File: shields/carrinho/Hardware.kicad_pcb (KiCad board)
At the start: 2 copper layers, 133.4 x 56.1 mm, 78 parts, among them J1 Conn_02x02_Odd_Even, J10 Conn_01x04, J11 Conn_01x04, J12 Conn_02x13_Odd_Even, J2 Conn_01x04, J3 Conn_02x02_Odd_Even, J4 Conn_01x02_Male, J5 Conn_01x02_Male, J6 Conn_01x02_Male, J7 Conn_01x02_Male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

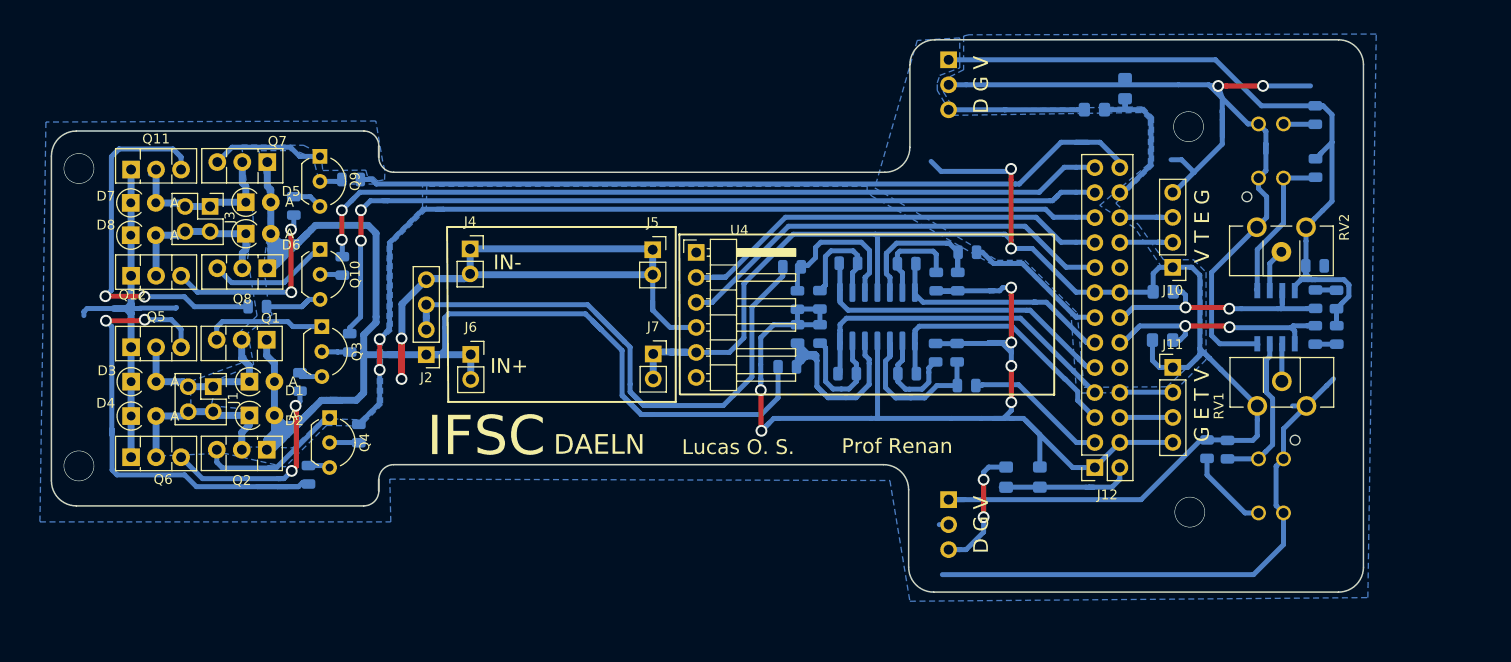
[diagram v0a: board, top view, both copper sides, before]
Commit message: Changed motors conector, added capacitor near ampop
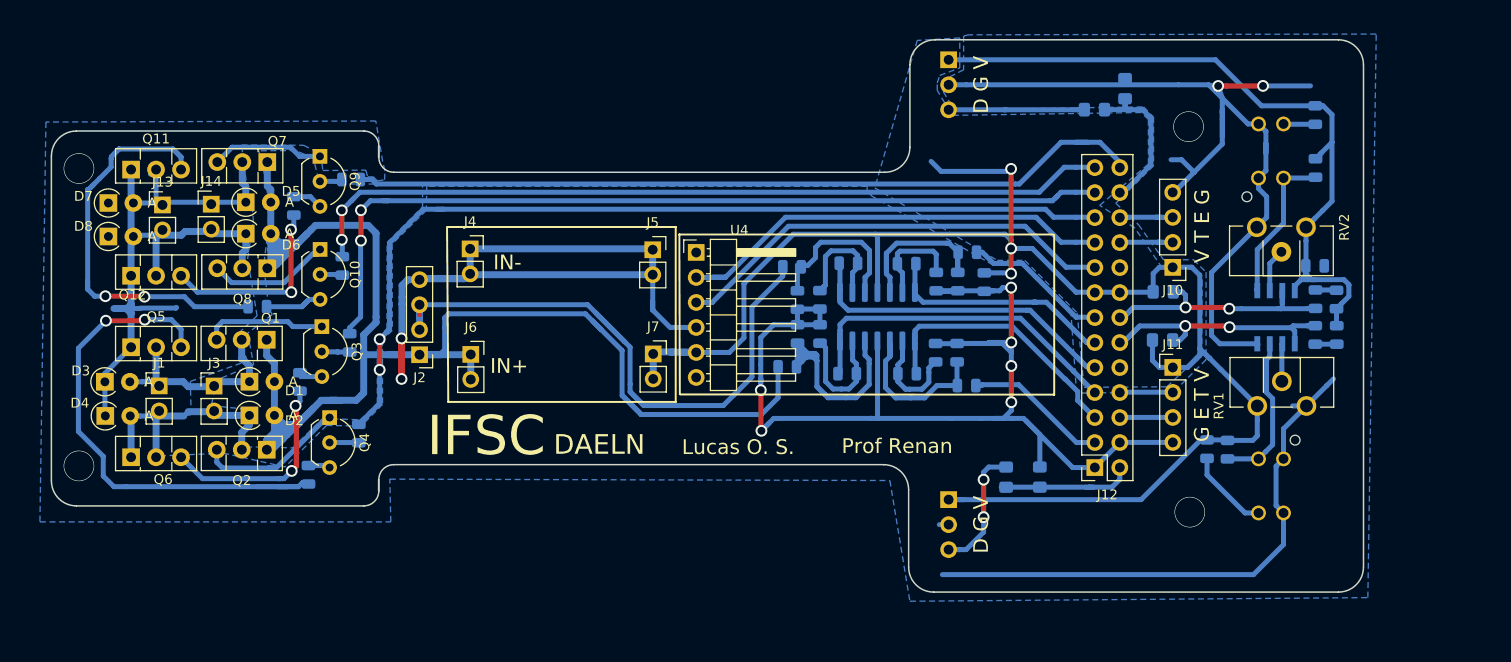
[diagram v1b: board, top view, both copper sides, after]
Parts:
- added C4: 100n, Capacitor_SMD:C_0805_2012Metric, B.Cu at (225.0, 56.4)
- added J13: Conn_01x02, Connector_PinHeader_2.54mm:PinHeader_1x02_P2.54mm_Vertical, F.Cu at (141.5, 48.5)
- added J14: Conn_01x02, Connector_PinHeader_2.54mm:PinHeader_1x02_P2.54mm_Vertical, F.Cu at (146.5, 48.5)
- C1, C2: value C -> 1n
- C3: value C -> 100n
- J1, J3: value Conn_02x02_Odd_Even -> Conn_01x02; footprint Connector_PinHeader_2.54mm:PinHeader_2x02_P2.54mm_Vertical -> Connector_PinHeader_2.54mm:PinHeader_1x02_P2.54mm_Vertical
- R31, R32: value R -> 10k
- moved J3 18.3 mm to (146.8, 67.0), turned to 0 degrees
- moved J1 5.49 mm to (141.2, 66.9), turned to 0 degrees
- moved D3 2.66 mm to (135.7, 66.5)
- moved D4 2.62 mm to (135.7, 70.0)
- moved D8 2.28 mm to (136.0, 51.8)
- moved D7 2.27 mm to (136.0, 48.3)
- moved J2 0.69 mm to (167.6, 63.8)
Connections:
- J3 pad 1: Net-(D5-Pad1) -> Net-(D1-Pad1)
- J3 pad 2: Net-(D6-Pad1) -> Net-(D2-Pad1)
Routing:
- net +5V: track 239.7 -> 244.8 mm, vias 2 -> 3
- net Net-(Q11-Pad3): track 39.8 -> 42.9 mm
- net GND: track 382.4 -> 379.6 mm
- net Net-(D1-Pad1): track 18.0 -> 20.7 mm
- net Net-(Q5-Pad3): track 51.9 -> 54.5 mm
- net Net-(D2-Pad1): track 17.2 -> 19.5 mm
- net Net-(D6-Pad1): track 19.3 -> 20.5 mm
- net BATMed: track 62.7 -> 63.7 mm

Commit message: Changed pots
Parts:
- RV1, RV2: footprint Potentiometer_THT:Potentiometer_Piher_PT-10-H01_Horizontal -> Potentiometer_THT:Potentiometer_Piher_PT-6-V_Vertical
- moved RV1 8.70 mm to (260.5, 64.9), turned to 180 degrees
- moved RV2 3.75 mm to (261.1, 49.1), turned to 180 degrees
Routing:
- net +5V: track 244.8 -> 253.2 mm
- net GND: track 379.6 -> 372.8 mm
- net Net-(RV2-Pad2): track 4.43 -> 6.52 mm
- net Net-(R28-Pad2): track 15.9 -> 16.9 mm
- net Net-(RV1-Pad2): track 3.83 -> 4.80 mm

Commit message: Updated car PCB
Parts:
- added D11: LED, LED_SMD:LED_0805_2012Metric, F.Cu at (221.3, 73.2)
- added D12: D_Schottky, Diode_SMD:D_SMB, B.Cu at (167.6, 70.6)
- added H1: MountingHole, MountingHole:MountingHole_3.2mm_M3, F.Cu at (262.7, 52.9)
- added H2: MountingHole, MountingHole:MountingHole_3.2mm_M3, F.Cu at (262.7, 66.9)
- added H3: MountingHole, MountingHole:MountingHole_3.2mm_M3, F.Cu at (134.4, 59.9)
- added R35: 1K, Resistor_SMD:R_0805_2012Metric, B.Cu at (217.2, 71.4)
- D10, D9: moved to F.Cu
- moved RV2 5.79 mm to (255.3, 49.3)
- moved RV1 3.77 mm to (256.8, 65.8)
- moved C3 3.60 mm to (256.5, 51.8), turned to 180 degrees
- moved D8 2.75 mm to (133.3, 51.6)
- moved D7 2.74 mm to (133.3, 48.3)
- moved D4 2.45 mm to (133.2, 70.1)
- moved D3 2.44 mm to (133.2, 66.9)
- moved R29 2.29 mm to (258.6, 61.8)
- moved R30 2.26 mm to (258.6, 58.2)
- moved D9 2.18 mm to (260.9, 61.8)
- moved D10 2.03 mm to (260.7, 58.2)
- moved J13 1.56 mm to (140.0, 48.5)
- moved J1 1.21 mm to (140.0, 67.2)
- moved R1 0.70 mm to (159.8, 62.5)
- moved J3 0.49 mm to (146.3, 66.8)
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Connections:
- J2 pad 1: +BATT -> Net-(D12-Pad2)
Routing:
- net GND: track 372.8 -> 301.9 mm
- net +BATT: track 166.9 -> 176.8 mm
- net R_TCRT: track 26.9 -> 33.0 mm, vias 2 -> 3
- net Net-(R28-Pad2): track 16.9 -> 22.2 mm
- net Net-(D2-Pad1): track 19.5 -> 24.3 mm
- net Net-(D12-Pad2): track 0.00 -> 4.70 mm
- net Net-(Q11-Pad3): track 42.9 -> 47.1 mm, vias 3 -> 0
- net Net-(D11-Pad1): track 0.00 -> 4.16 mm, vias 0 -> 1
- net Net-(D9-Pad2): track 2.18 -> 6.22 mm, vias 0 -> 1
- net Net-(D1-Pad1): track 20.7 -> 24.7 mm
- net Net-(D5-Pad1): track 19.8 -> 23.2 mm
- net Net-(R26-Pad2): track 15.8 -> 19.2 mm
- net Net-(D6-Pad1): track 20.5 -> 23.8 mm
- net Net-(D10-Pad2): track 2.15 -> 5.34 mm, vias 0 -> 1
- net +5V: track 253.2 -> 250.3 mm, vias 3 -> 5
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- added copper zone on F.Cu, net GND
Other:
- board size 133.4 x 56.1 mm -> 135.8 x 56.1 mm
